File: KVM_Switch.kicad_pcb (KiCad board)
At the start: 4 copper layers, 100 x 70 mm, 110 parts, among them J1 HDMI_A, J2 HDMI_A, J3 HDMI_A, J4 USB_C_Receptacle_USB2.0_16P, J5 USB_C_Receptacle_USB2.0_16P, J6 USB_C_Receptacle_USB2.0_16P, J7 USB_A_Stacked, J8 USB_A_Stacked, SW1 SPST-NO, U1 TPD4E02B04DQA, U10 USBLC6-2SC6, U11 TS3USB221AQRSERQ1, U12 USBLC6-2SC6, U13 USB2514B_Bi, U14 USBLC6-2SC6, U15 USBLC6-2SC6, U16 USBLC6-2SC6, U17 USBLC6-2SC6, U2 TPD4E02B04DQA, U3 TPD4E02B04DQA, U4 TPD4E02B04DQA, U5 HD3SS215RTQR, U6 TPD4E02B04DQA, U7 TPD4E02B04DQA, U8 TLV75533PDBV, U9 STM32C031G6Ux, X1 24MHz

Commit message: New layout & set stackup
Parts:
- moved J6 66.5 mm to (145.0, 132.0), turned to 0 degrees
- moved R13 62.2 mm to (185.4, 101.0), turned to 180 degrees
- moved J2 62.0 mm to (122.0, 129.0), turned to -90 degrees
- moved C6 60.9 mm to (184.9, 99.0), turned to 180 degrees
- moved R20 59.1 mm to (140.0, 126.0), turned to 90 degrees
- moved R21 56.9 mm to (142.5, 126.0), turned to 90 degrees
- moved TP8 56.3 mm to (178.4, 107.9), turned to 180 degrees
- moved R9 55.3 mm to (115.0, 121.0), turned to 90 degrees
- moved U9 54.4 mm to (180.4, 98.0), turned to 180 degrees
- moved TP14 54.3 mm to (178.4, 104.4), turned to 180 degrees
- moved R2 53.3 mm to (118.0, 122.0), turned to 90 degrees
- moved TP9 52.6 mm to (175.4, 108.0), turned to 180 degrees
- moved U12 51.3 mm to (145.0, 124.0), turned to 90 degrees
- moved TP10 50.4 mm to (175.4, 104.5), turned to 180 degrees
- moved TP4 49.7 mm to (117.0, 119.0), turned to -90 degrees
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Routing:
- net /HDMI_Switch/HDMI_IN_A/CK_N: track 0.00 -> 33.7 mm
- net /HDMI_Switch/HDMI_IN_A/CK_P: track 0.00 -> 33.4 mm
- net /HDMI_Switch/HDMI_IN_A/D0_N: track 0.00 -> 32.5 mm
- net /HDMI_Switch/HDMI_IN_A/D0_P: track 0.00 -> 32.2 mm
- net /HDMI_Switch/HDMI_IN_A/D1_N: track 0.00 -> 31.4 mm
- net /HDMI_Switch/HDMI_IN_A/D1_P: track 0.00 -> 31.1 mm
- net /HDMI_Switch/HDMI_IN_A/D2_N: track 0.00 -> 30.2 mm
- net /HDMI_Switch/HDMI_IN_A/D2_P: track 0.00 -> 29.9 mm
- net /HDMI_Switch/HDMI_OUT/D2_P: track 0.00 -> 2.99 mm, vias 0 -> 1
- net /HDMI_Switch/HDMI_OUT/D2_N: track 0.00 -> 2.07 mm, vias 0 -> 1

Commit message: Placed Connectors where i want them - I thnik
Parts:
- J7, J8: footprint Connector_USB:USB_A_Wuerth_61400826021_Horizontal_Stacked -> KVM_Swtich:USB_A_Wuerth_61400826021_Horizontal_Stacked
- moved C25 11.3 mm to (184.4, 141.3)
- moved J8 8.73 mm to (168.5, 70.0)
- moved J7 8.54 mm to (168.0, 130.0)
- moved C7 4.47 mm to (188.0, 83.5)
- moved R14 4.47 mm to (186.0, 80.5)
- moved R15 4.47 mm to (188.0, 80.5)
- moved C10 4.00 mm to (189.0, 102.9)
- moved C11 4.00 mm to (189.0, 109.0)
- moved C12 4.00 mm to (189.0, 115.0)
- moved C8 4.00 mm to (189.0, 91.0)
- moved C9 4.00 mm to (189.0, 97.0)
- moved D2 3.16 mm to (194.0, 91.0)
- moved D3 3.16 mm to (194.0, 97.0)
- moved D4 3.16 mm to (194.0, 103.0)
- moved D5 3.16 mm to (194.0, 109.0)
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
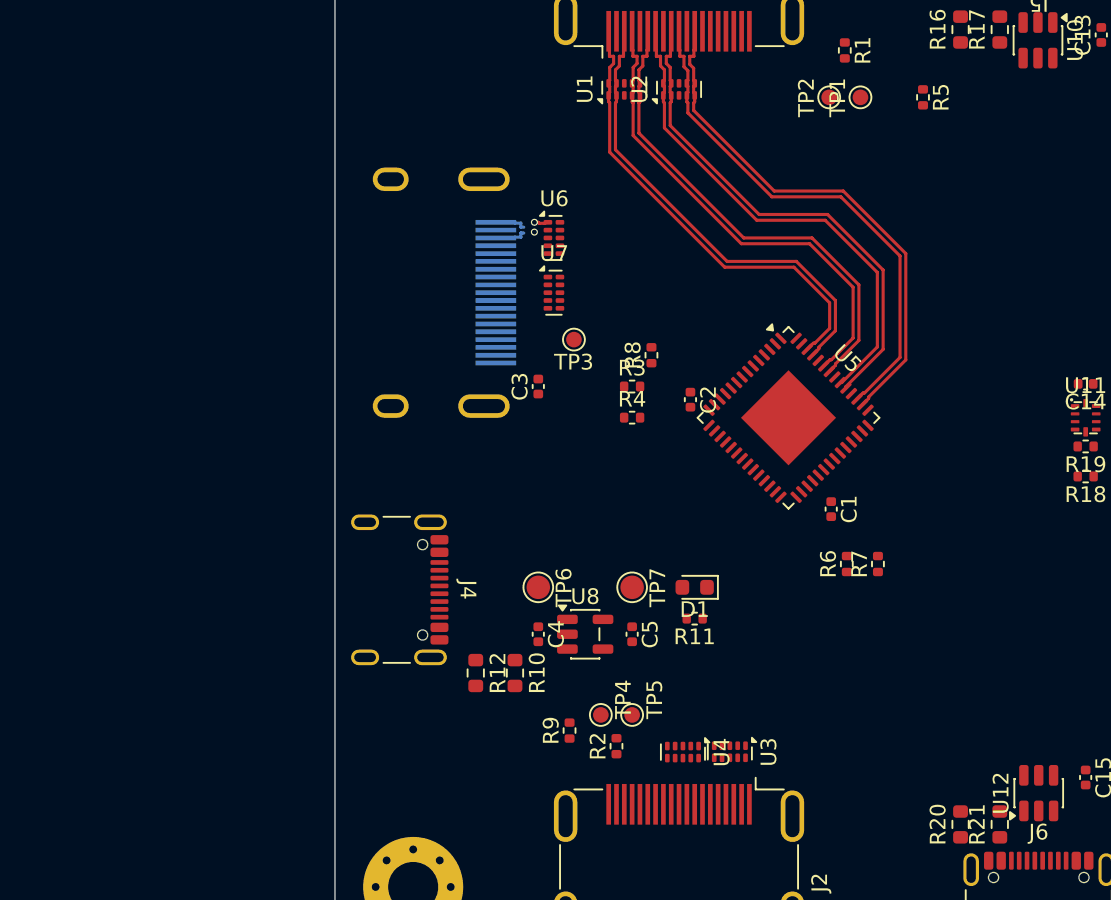
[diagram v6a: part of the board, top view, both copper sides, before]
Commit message: Routed HDMI TMDS
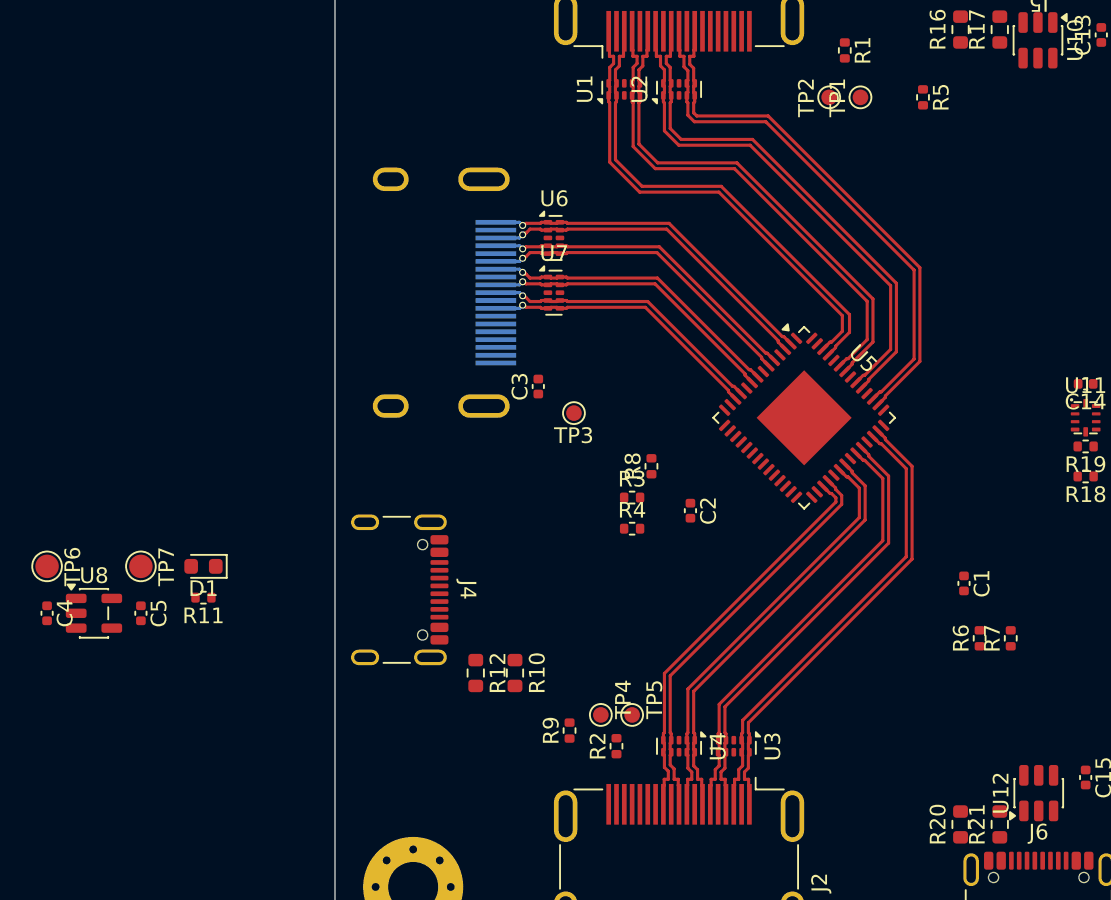
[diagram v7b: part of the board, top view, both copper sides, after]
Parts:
- moved C4 31.4 mm to (81.6, 112.5)
- moved C5 31.4 mm to (87.6, 112.5)
- moved D1 31.4 mm to (91.6, 109.5)
- moved R11 31.4 mm to (91.6, 111.5)
- moved TP6 31.4 mm to (81.6, 109.5)
- moved TP7 31.4 mm to (87.6, 109.5)
- moved U8 31.4 mm to (84.6, 112.5)
- moved R7 9.73 mm to (143.2, 114.1)
- moved C1 9.73 mm to (140.2, 110.6)
- moved R6 9.73 mm to (141.2, 114.1)
- moved R4 7.10 mm to (119.0, 107.1)
- moved C2 7.10 mm to (122.7, 105.9)
- moved R3 7.10 mm to (119.0, 105.1)
- moved R8 7.10 mm to (120.2, 103.1)
- moved TP3 4.70 mm to (115.3, 99.7)
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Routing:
- net /HDMI_Switch/HDMI_IN_B/D2_P: track 0.00 -> 29.6 mm
- net /HDMI_Switch/HDMI_IN_B/D2_N: track 0.00 -> 29.3 mm
- net /HDMI_Switch/HDMI_IN_B/D1_P: track 0.00 -> 28.4 mm
- net /HDMI_Switch/HDMI_IN_B/D1_N: track 0.00 -> 28.1 mm
- net /HDMI_Switch/HDMI_IN_B/D0_P: track 0.00 -> 27.3 mm
- net /HDMI_Switch/HDMI_IN_B/D0_N: track 0.00 -> 27.0 mm
- net /HDMI_Switch/HDMI_IN_B/CK_P: track 0.00 -> 26.1 mm
- net /HDMI_Switch/HDMI_IN_B/CK_N: track 0.00 -> 25.8 mm
- net /HDMI_Switch/HDMI_OUT/D1_P: track 0.00 -> 21.2 mm, vias 0 -> 1
- net /HDMI_Switch/HDMI_OUT/D1_N: track 0.00 -> 21.0 mm, vias 0 -> 1
- net /HDMI_Switch/HDMI_OUT/D2_N: track 2.07 -> 22.2 mm
- net /HDMI_Switch/HDMI_OUT/D0_P: track 0.00 -> 19.8 mm, vias 0 -> 1
- net /HDMI_Switch/HDMI_OUT/D2_P: track 2.99 -> 22.4 mm
- net /HDMI_Switch/HDMI_OUT/D0_N: track 0.00 -> 19.4 mm, vias 0 -> 1
- net /HDMI_Switch/HDMI_OUT/CK_P: track 0.00 -> 18.6 mm, vias 0 -> 1
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
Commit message: TMDS length matching *not done
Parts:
- moved R7 31.4 mm to (125.0, 88.5), turned to 135 degrees
- moved R6 28.2 mm to (126.5, 90.0), turned to 135 degrees
- moved C1 16.3 mm to (125.8, 103.2), turned to -45 degrees
- moved C2 14.9 mm to (131.2, 93.7), turned to 135 degrees
- moved R8 13.8 mm to (128.9, 92.4), turned to 135 degrees
- moved TP3 10.3 mm to (107.0, 93.5)
- moved R5 8.55 mm to (129.1, 78.6), turned to 90 degrees
- moved R4 7.19 mm to (126.2, 106.3), turned to 135 degrees
- moved TP2 6.22 mm to (125.4, 79.0)
- moved R1 5.05 mm to (128.0, 78.6)
- moved R3 4.25 mm to (122.6, 102.8), turned to 135 degrees
- moved C3 2.46 mm to (114.0, 95.8)
- moved R9 2.15 mm to (116.9, 121.0), turned to -90 degrees
- moved TP1 1.75 mm to (132.1, 78.6)
- moved TP4 1.04 mm to (116.7, 118.0)
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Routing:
- net /HDMI_Switch/HDMI_IN_A/SCL: track 0.00 -> 34.1 mm, vias 0 -> 2
- net /HDMI_Switch/HDMI_IN_A/SDA: track 0.00 -> 33.5 mm, vias 0 -> 2
- net /HDMI_Switch/HDMI_OUT/SDA: track 0.00 -> 25.9 mm, vias 0 -> 1
- net /HDMI_Switch/HDMI_IN_B/SDA: track 0.00 -> 25.6 mm, vias 0 -> 2
- net /HDMI_Switch/HDMI_IN_B/SCL: track 0.00 -> 25.4 mm, vias 0 -> 2
- net /HDMI_Switch/HDMI_OUT/SCL: track 0.00 -> 20.7 mm, vias 0 -> 1
- net /HDMI_Switch/HDMI_OUT/HPD: track 0.00 -> 16.7 mm, vias 0 -> 1
- net Net-(U5-AUX_SEL): track 0.00 -> 7.78 mm
- net GND: track 0.00 -> 7.65 mm, vias 0 -> 5
- net /HDMI_Switch/HDMI_IN_B/CEC: track 0.00 -> 7.46 mm
- net VBUS: track 0.00 -> 5.45 mm, vias 0 -> 3
- net /HDMI_Switch/DET_A: track 0.00 -> 5.11 mm
- net /HDMI_Switch/HDMI_IN_A/HPD: track 0.00 -> 4.99 mm
- net /HDMI_Switch/HDMI_IN_A/CEC: track 0.00 -> 4.97 mm
- net Net-(J1-+5V): track 0.00 -> 4.34 mm
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- added copper zone on B.Cu, net GND
- added copper zone on F.Cu, net GND
- added copper zone on In1.Cu, net GND
